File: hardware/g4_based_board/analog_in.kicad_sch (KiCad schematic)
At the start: 16 parts, among them J12 Screw_Terminal_01x04, U4 TL074

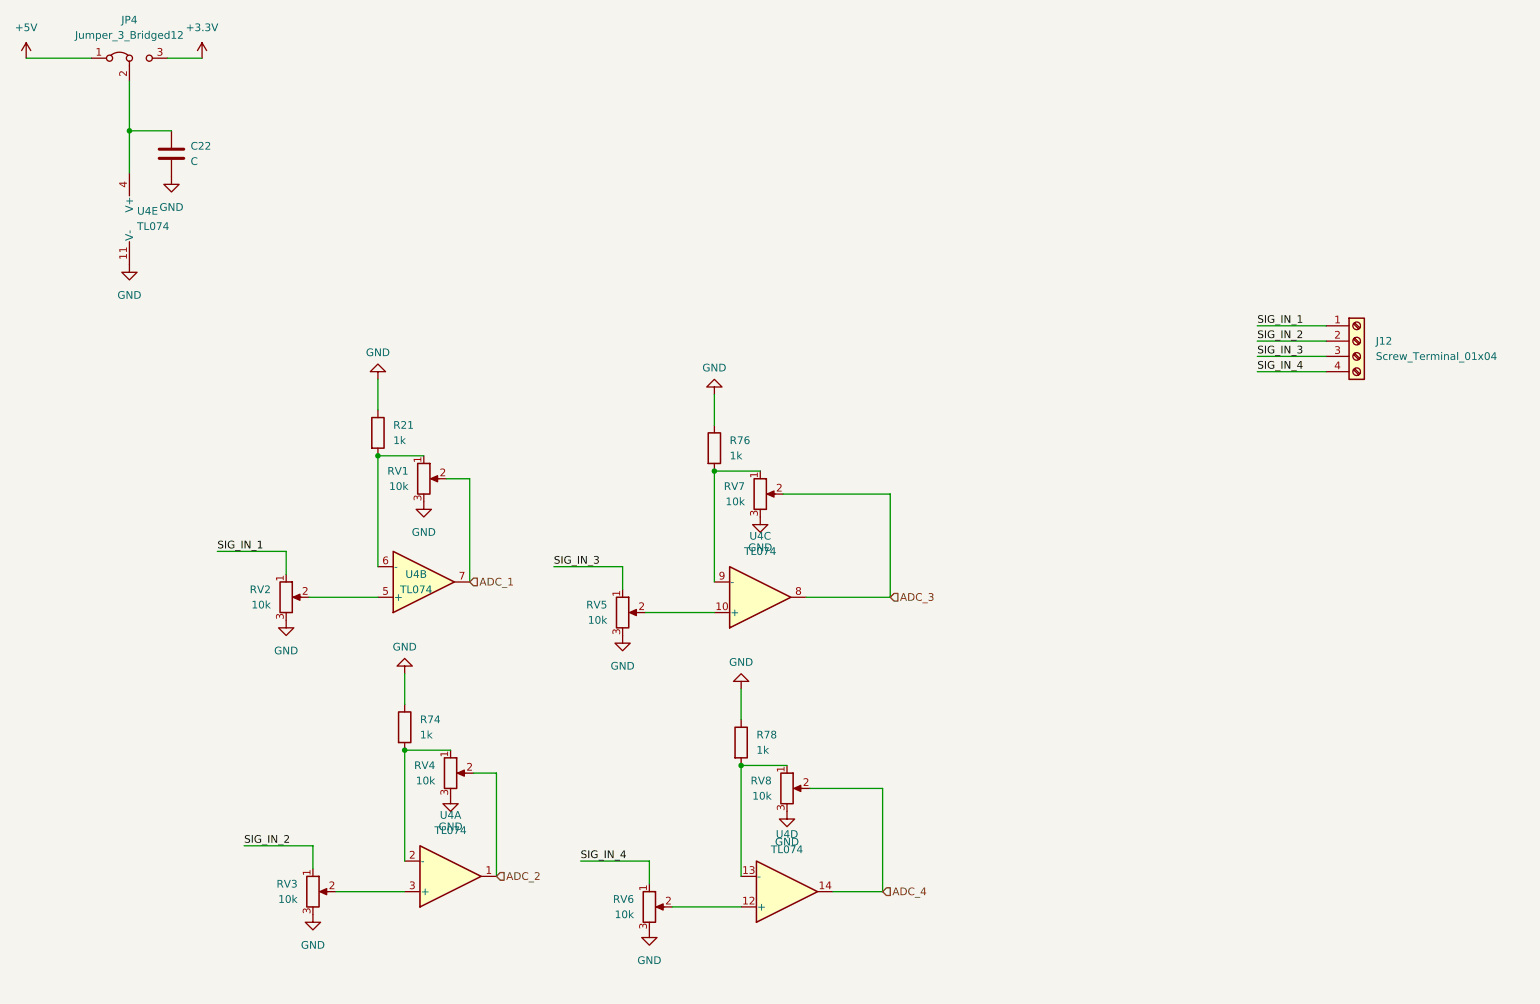
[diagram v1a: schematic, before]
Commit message: minor addtion and swd header added and usart removed
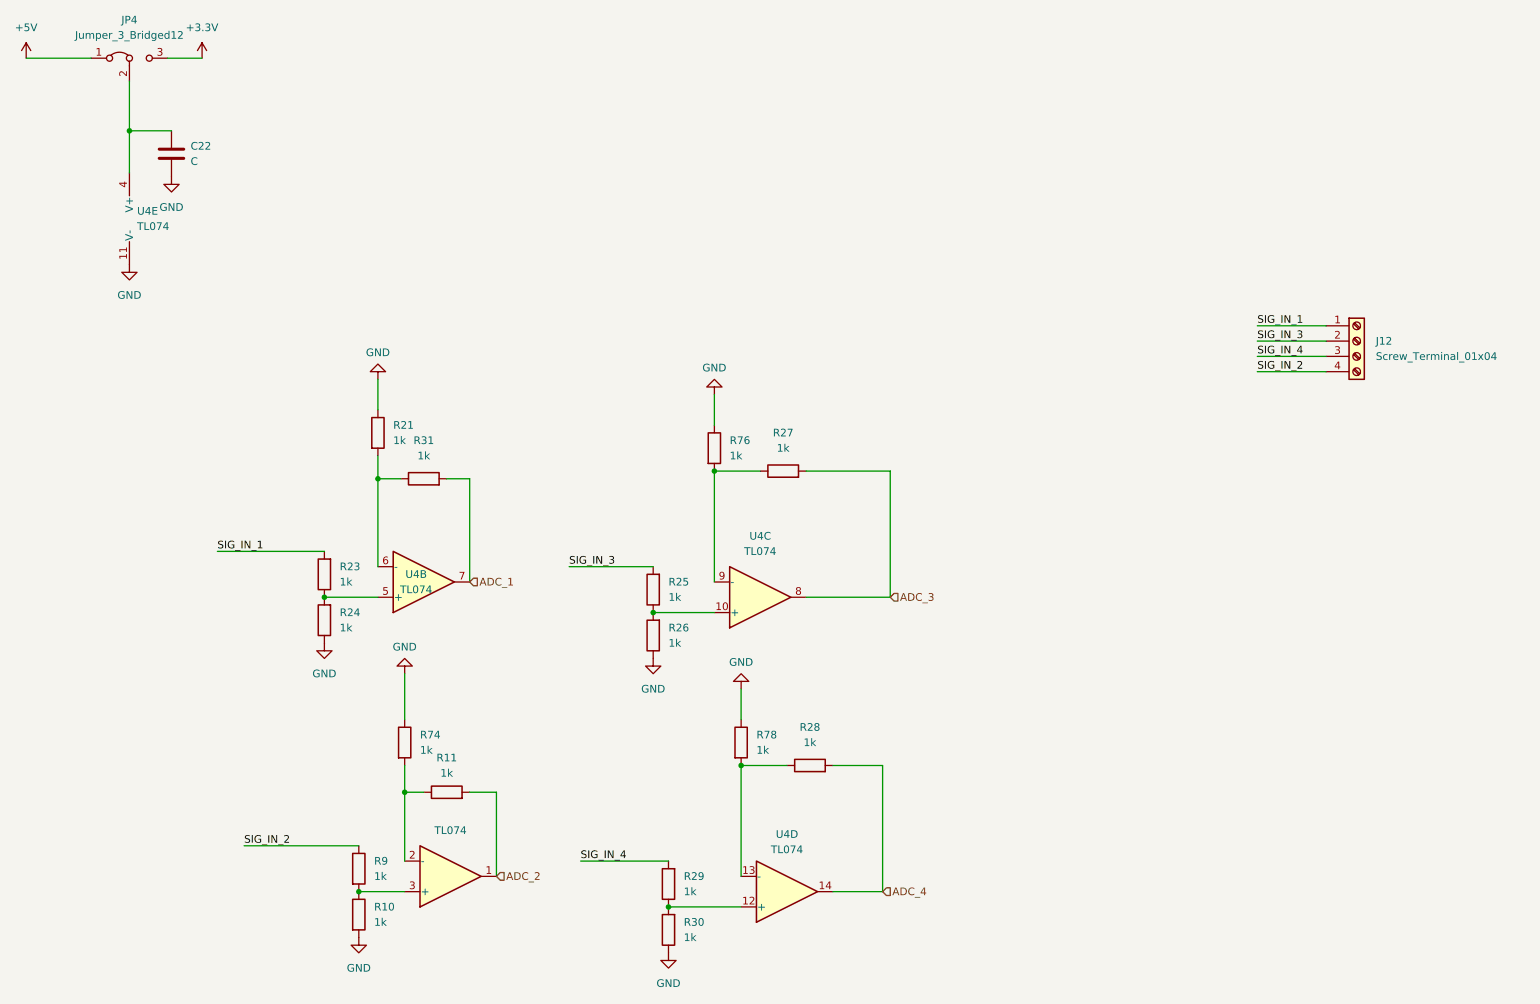
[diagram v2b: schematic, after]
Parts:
- removed RV1, RV2, RV3, RV4, RV5, RV6, RV7, RV8: 10k, Potentiometer_THT:Potentiometer_Vishay_T73YP_Vertical, symbol Device:R_Potentiometer
- added R10, R11, R23, R24, R25, R26, R27, R28, R29, R30, R31, R9: 1k, Resistor_SMD:R_0603_1608Metric_Pad0.98x0.95mm_HandSolder, symbol Device:R
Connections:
- net ADC_1: now also R31.2
- net ADC_2: now also R11.2
- net ADC_3: now also R27.2
- net ADC_4: now also R28.2
- net GND: now also R10.2, R24.1, R26.1, R30.1
- net SIG_IN_1: now also R23.2
- net SIG_IN_2: now also J12.4 (Pin_4), R9.1; no longer J12.2 (Pin_2)
- net SIG_IN_3: now also J12.2 (Pin_2), R25.2; no longer J12.3 (Pin_3)
- net SIG_IN_4: now also J12.3 (Pin_3), R29.2; no longer J12.4 (Pin_4)
- net at R78.2, U4.13 (-): now also R28.1
- net at U4.3 (+): now also R10.1, R9.2
- net at U4.12 (+): now also R29.1, R30.2
- net at R74.2, U4.2 (-): now also R11.1
- net at R76.2, U4.9 (-): now also R27.1
- net at R21.2, U4.6 (-): now also R31.1
- net at U4.5 (+): now also R23.1, R24.2
- net at U4.10 (+): now also R25.1, R26.2
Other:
- moved on the sheet: R74
